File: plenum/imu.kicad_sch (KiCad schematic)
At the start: 1 part, among them U20 BMI270

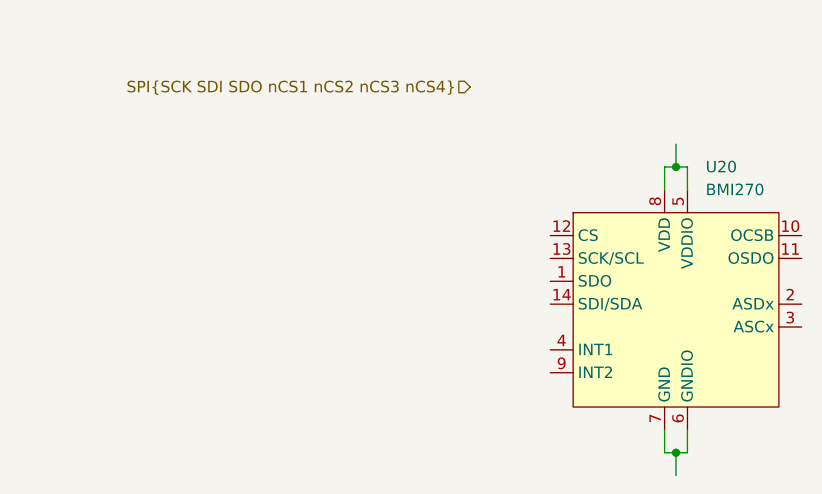
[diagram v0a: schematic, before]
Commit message: adding housekeeping board
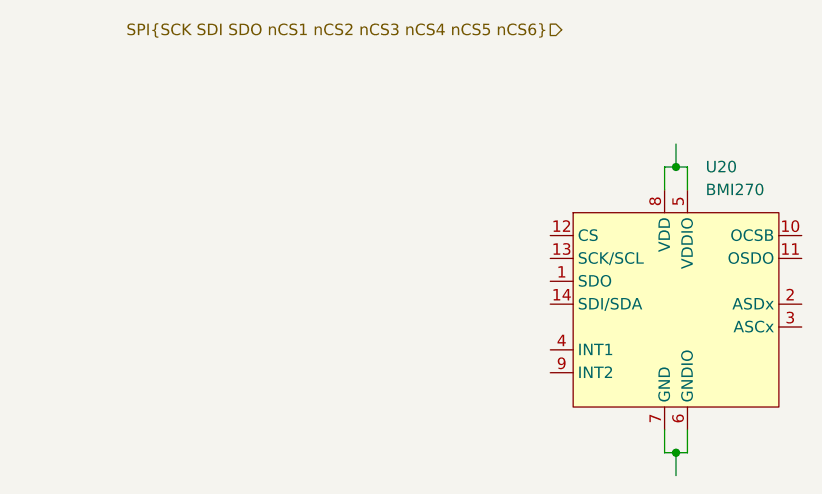
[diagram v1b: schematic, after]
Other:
- company: (none) -> University of Minnesota
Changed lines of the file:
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@@
-(kicad_sch (version 20211123) (generator eeschema)
+(kicad_sch (version 20230121) (generator eeschema)
   (paper "A4")
+  (title_block
+    (rev "1")
+    (company "University of Minnesota")
+    (comment 1 "Author: Thanasi Pantazides, panta013@umn.edu")
+  )
   (junction (at 82.55 69.85) (diameter 0) (color 0 0 0 0)
   )
@@
   )
   (wire (pts (xy 81.28 40.64) (xy 81.28 38.1))
-    (stroke (width 0) (type default) (color 0 0 0 0))
+    (stroke (width 0) (type default))
   )
   (wire (pts (xy 82.55 38.1) (xy 83.82 38.1))
-    (stroke (width 0) (type default) (color 0 0 0 0))
+    (stroke (width 0) (type default))
   )
   (wire (pts (xy 81.28 67.31) (xy 81.28 69.85))
-    (stroke (width 0) (type default) (color 0 0 0 0))
+    (stroke (width 0) (type default))
   )
   (wire (pts (xy 82.55 35.56) (xy 82.55 38.1))
-    (stroke (width 0) (type default) (color 0 0 0 0))
+    (stroke (width 0) (type default))
   )
   (wire (pts (xy 81.28 38.1) (xy 82.55 38.1))
-    (stroke (width 0) (type default) (color 0 0 0 0))
+    (stroke (width 0) (type default))
   )
   (wire (pts (xy 82.55 69.85) (xy 83.82 69.85))
-    (stroke (width 0) (type default) (color 0 0 0 0))
+    (stroke (width 0) (type default))
   )
   (wire (pts (xy 83.82 38.1) (xy 83.82 40.64))
-    (stroke (width 0) (type default) (color 0 0 0 0))
+    (stroke (width 0) (type default))
   )
   (wire (pts (xy 82.55 69.85) (xy 82.55 72.39))
-    (stroke (width 0) (type default) (color 0 0 0 0))
+    (stroke (width 0) (type default))
   )
   (wire (pts (xy 81.28 69.85) (xy 82.55 69.85))
-    (stroke (width 0) (type default) (color 0 0 0 0))
+    (stroke (width 0) (type default))
   )
   (wire (pts (xy 83.82 69.85) (xy 83.82 67.31))
-    (stroke (width 0) (type default) (color 0 0 0 0))
+    (stroke (width 0) (type default))
   )
-  (hierarchical_label "SPI{SCK SDI SDO nCS1 nCS2 nCS3 nCS4}" (shape input) (at 59.69 29.21 180)
+  (hierarchical_label "SPI{SCK SDI SDO nCS1 nCS2 nCS3 nCS4 nCS5 nCS6}" (shape input) (at 69.85 22.86 180) (fields_autoplaced)
     (effects (font (size 1.27 1.27)) (justify right))
   )
   (symbol (lib_id "Sensor_Motion:BMI270") (at 82.55 43.18 0) (unit 1)
-    (in_bom yes) (on_board yes) (fields_autoplaced)
-    (property "Reference" "U20" (id 0) (at 85.8394 38.1 0)
+    (in_bom yes) (on_board yes) (dnp no) (fields_autoplaced)
+    (property "Reference" "U20" (at 85.8394 38.1 0)
       (effects (font (size 1.27 1.27)) (justify left))
     )
-    (property "Value" "BMI270" (id 1) (at 85.8394 40.64 0)
+    (property "Value" "BMI270" (at 85.8394 40.64 0)
       (effects (font (size 1.27 1.27)) (justify left))
     )
-    (property "Footprint" "Sensor_Motion:BMI270" (id 2) (at 82.55 46.99 0)
+    (property "Footprint" "Sensor_Motion:BMI270" (at 82.55 46.99 0)
       (effects (font (size 1.27 1.27)) hide)
     )
-    (property "Datasheet" "https://www.bosch-sensortec.com/media/boschsensortec/downloads/datasheets/bst-bmi270-ds000.pdf" (id 3) (at 81.28 43.18 0)
+    (property "Datasheet" "https://www.bosch-sensortec.com/media/boschsensortec/downloads/datasheets/bst-bmi270-ds000.pdf" (at 81.28 43.18 0)
       (effects (font (size 1.27 1.27)) hide)
     )
-    (property "Digikey" "828-1091-1-ND" (id 4) (at 82.55 43.18 0)
+    (property "Digikey" "828-1091-1-ND" (at 82.55 43.18 0)
       (effects (font (size 1.27 1.27)) hide)
     )
@@
     (pin "8")
     (pin "9")
+    (instances
+      (project "plenum"
+        (path "/fb761b7c-8700-4d95-9165-a5a771518450/9fb1c949-1824-4556-ba18-a9edd64fb2ac"
+          (reference "U20") (unit 1)
+        )
+      )
+    )
   )
 )
